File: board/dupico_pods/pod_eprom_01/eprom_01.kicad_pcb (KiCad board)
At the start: 2 copper layers, 20.4 x 53.9 mm, 19 parts, among them J1 dupico, J2 ROM Socket, Q1 MMBT3906, Q2 MMBT3906, Q3 MMBT3906, Q4 MMBT3906, Q5 MMBT3906, Q6 MMBT3906, Q7 MMBT3906, U2 74ACT138

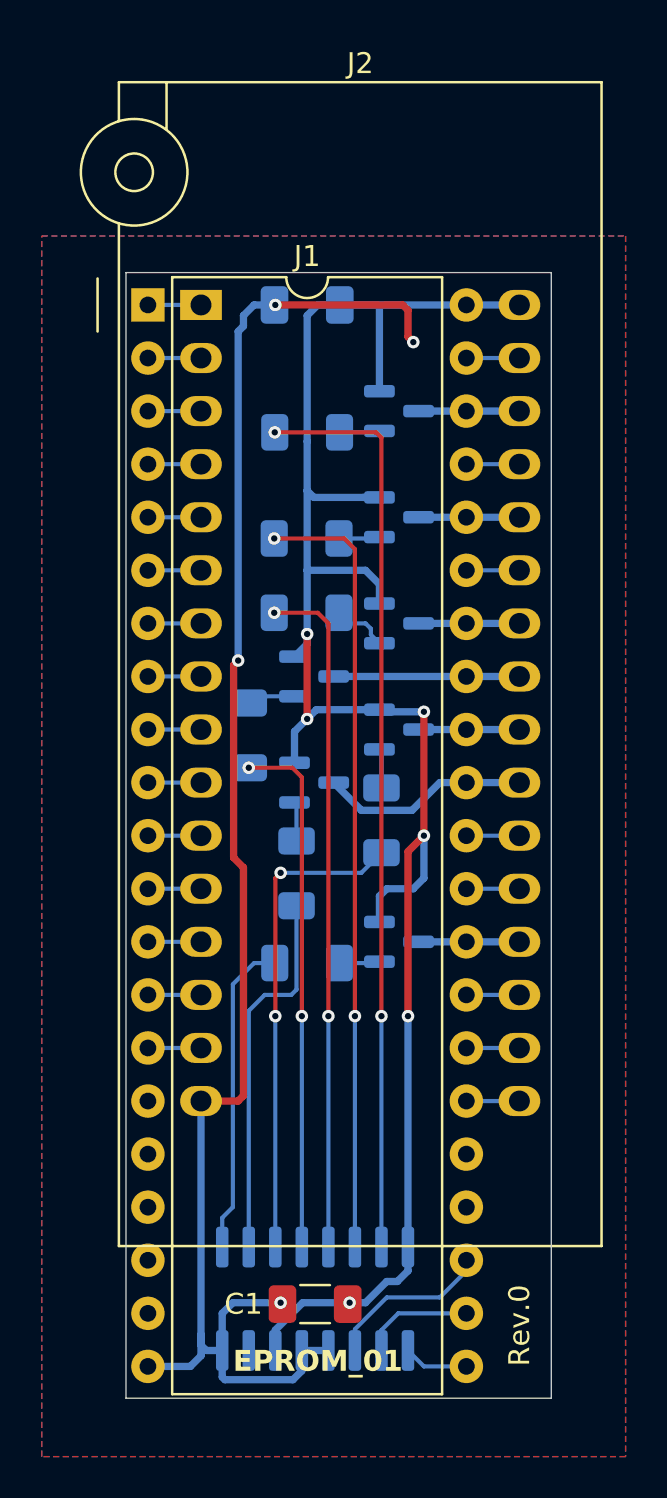
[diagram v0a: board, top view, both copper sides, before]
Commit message: Shift the ZIF32 socket on the eprom_01 pod
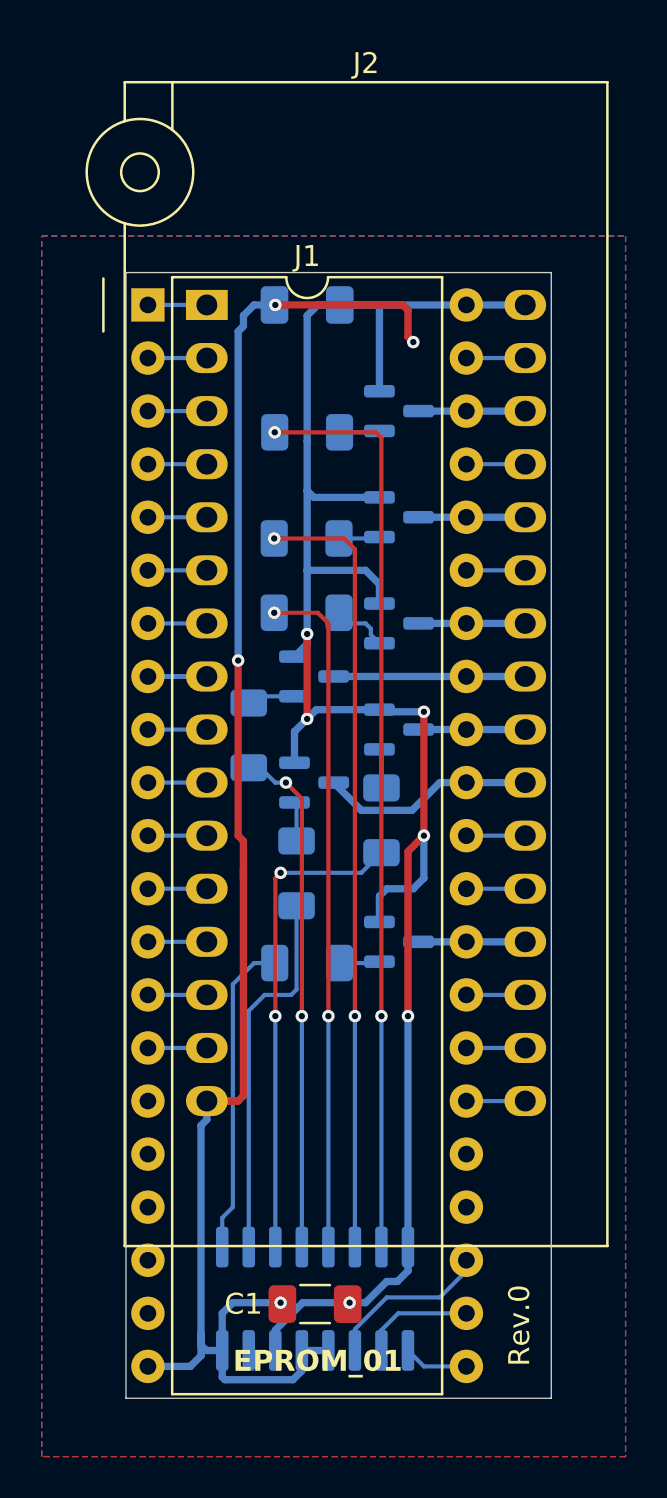
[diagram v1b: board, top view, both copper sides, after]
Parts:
- moved J2 0.28 mm to (150.1, 49.0)
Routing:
- net /ZIF_8: track 2.54 -> 6.13 mm
- net GND: track 78.6 -> 80.3 mm
- net /~{PWR_3}: track 25.2 -> 24.6 mm
